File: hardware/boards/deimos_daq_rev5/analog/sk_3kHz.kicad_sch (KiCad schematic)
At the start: 6 parts, among them U45001 OPA333xxDBV

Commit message: put +/12V on all inamps. add 3.3V zener behind first resistor of each filter.
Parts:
- added D15001: BZT52C3V3, Diode_SMD:D_SOD-323, symbol Device:D_Zener
- renumbered C45001 to C29001, C45002 to C29002, C45003 to C29003, R45001 to R29001, R45002 to R29002, U45001 to U29001
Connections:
- net GND: now also D15001.2 (A)
- net at C29002.1, R29001.2, R29002.1: now also D15001.1 (K)

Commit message: add stabilizing integrator to current sinks
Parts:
- renumbered C29001 to C27001, C29002 to C27002, C29003 to C27003, D15001 to D17001, R29001 to R27001, R29002 to R27002, U29001 to U27001
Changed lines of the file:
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@@
 		(on_board yes)
 		(dnp no)
-		(property "Reference" "C29001"
+		(property "Reference" "C27001"
 			(at 98.552 96.774 90)
 			(effects
@@
 		(on_board yes)
 		(dnp no)
-		(property "Reference" "C29003"
+		(property "Reference" "C27003"
 			(at 116.078 76.2 90)
 			(effects
@@
 		(on_board yes)
 		(dnp no)
-		(property "Reference" "R29001"
+		(property "Reference" "R27001"
 			(at 82.55 77.343 90)
 			(effects
@@
 		(on_board yes)
 		(dnp no)
-		(property "Reference" "#PWR193"
+		(property "Reference" "#PWR188"
 			(at 113.03 99.06 0)
 			(effects
@@
 		(on_board yes)
 		(dnp no)
-		(property "Reference" "D15001"
+		(property "Reference" "D17001"
 			(at 85.09 86.614 0)
 			(effects
@@
 		(on_board yes)
 		(dnp no)
-		(property "Reference" "U29001"
+		(property "Reference" "U27001"
 			(at 121.158 89.916 0)
 			(effects
@@
 		(on_board yes)
 		(dnp no)
-		(property "Reference" "#PWR192"
+		(property "Reference" "#PWR187"
 			(at 120.65 83.82 0)
 			(effects
@@
 		(on_board yes)
 		(dnp no)
-		(property "Reference" "R29002"
+		(property "Reference" "R27002"
 			(at 93.98 77.343 90)
 			(effects
@@
 		(on_board yes)
 		(dnp no)
-		(property "Reference" "#PWR15005"
+		(property "Reference" "#PWR17005"
 			(at 87.376 96.52 0)
 			(effects
@@
 		(on_board yes)
 		(dnp no)
-		(property "Reference" "C29002"
+		(property "Reference" "C27002"
 			(at 110.998 58.674 0)
 			(effects
@@
 		(on_board yes)
 		(dnp no)
-		(property "Reference" "#PWR191"
+		(property "Reference" "#PWR186"
 			(at 116.84 72.39 0)
 			(effects
@@
 		(on_board yes)
 		(dnp no)
-		(property "Reference" "#PWR190"
+		(property "Reference" "#PWR185"
 			(at 101.6 99.06 0)
 			(effects

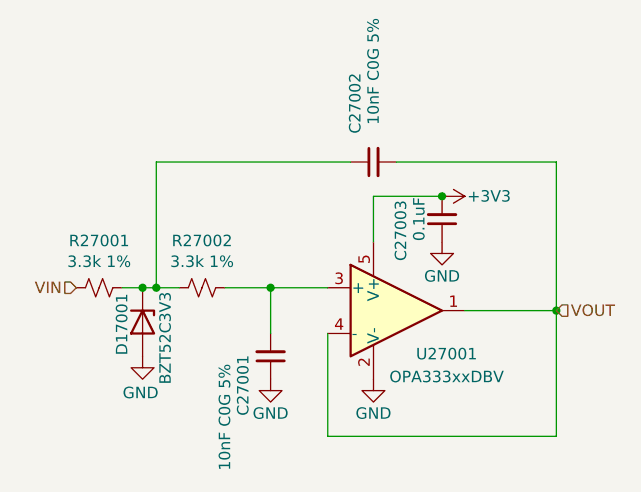
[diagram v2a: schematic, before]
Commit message: use opa196 with split rail instead of opa333 with single rail. replace zeners.
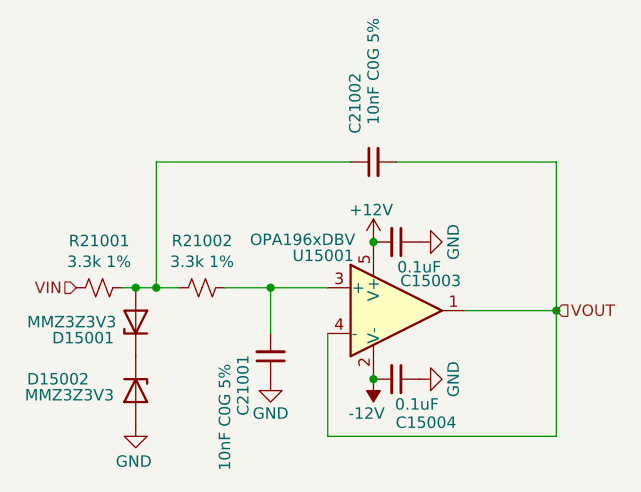
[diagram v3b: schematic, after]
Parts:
- removed C27003: 0.1uF, Capacitor_SMD:C_0402_1005Metric, symbol Device:C_Small
- removed D17001: BZT52C3V3, Diode_SMD:D_SOD-323, symbol Device:D_Zener
- removed U27001: OPA333xxDBV, Package_TO_SOT_SMD:SOT-23-5, symbol Amplifier_Operational:OPA333xxDBV
- added C15003, C15004: 0.1uF, Capacitor_SMD:C_0402_1005Metric, symbol Device:C_Small
- added D15001, D15002: MMZ3Z3V3, Diode_SMD:D_SOD-323, symbol Device:D_Zener
- added U15001: OPA196xDBV, Package_TO_SOT_SMD:SOT-23-5, symbol Amplifier_Operational:OPA196xDBV
- renumbered C27001 to C21001, C27002 to C21002, R27001 to R21001, R27002 to R21002
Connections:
- net GND: now also C15003.1, C15004.1, D15002.2 (A)
- net VOUT: now also U15001.1, U15001.4 (-)
- net at C21001.2, R21002.2: now also U15001.3 (+)
- net at C21002.1, R21001.2, R21002.1: now also D15001.2 (A)
- new net: D15001.1 (K), D15002.1 (K)
- new net +12V: C15003.2, U15001.5 (V+)
- new net -12V: C15004.2, U15001.2 (V-)

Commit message: remove unnecessary amps and buffers
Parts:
- renumbered C15003 to C17003, C15004 to C17004, C21001 to C47001, C21002 to C47002, D15001 to D17001, D15002 to D17002, R21001 to R47001, R21002 to R47002, U15001 to U17001
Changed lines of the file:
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@@
 		(on_board yes)
 		(dnp no)
-		(property "Reference" "#PWR15004"
+		(property "Reference" "#PWR17004"
 			(at 113.03 88.9 0)
 			(effects
@@
 		(on_board yes)
 		(dnp no)
-		(property "Reference" "C21001"
+		(property "Reference" "C47001"
 			(at 98.552 96.774 90)
 			(effects
@@
 		(on_board yes)
 		(dnp no)
-		(property "Reference" "D15002"
+		(property "Reference" "D17002"
 			(at 77.978 92.71 90)
 			(effects
@@
 		(on_board yes)
 		(dnp no)
-		(property "Reference" "D15001"
+		(property "Reference" "D17001"
 			(at 80.772 88.138 90)
 			(effects
@@
 		(on_board yes)
 		(dnp no)
-		(property "Reference" "#PWR15002"
+		(property "Reference" "#PWR17002"
 			(at 86.614 104.14 0)
 			(effects
@@
 		(on_board yes)
 		(dnp no)
-		(property "Reference" "R21001"
+		(property "Reference" "R47001"
 			(at 82.55 77.343 90)
 			(effects
@@
 		(on_board yes)
 		(dnp no)
-		(property "Reference" "#PWR15006"
+		(property "Reference" "#PWR17006"
 			(at 124.46 92.71 0)
 			(effects
@@
 		(on_board yes)
 		(dnp no)
-		(property "Reference" "#PWR15005"
+		(property "Reference" "#PWR17005"
 			(at 124.46 77.47 0)
 			(effects
@@
 		(on_board yes)
 		(dnp no)
-		(property "Reference" "U15001"
+		(property "Reference" "U17001"
 			(at 107.442 78.994 0)
 			(effects
@@
 		(on_board yes)
 		(dnp no)
-		(property "Reference" "R21002"
+		(property "Reference" "R47002"
 			(at 93.98 77.343 90)
 			(effects
@@
 		(on_board yes)
 		(dnp no)
-		(property "Reference" "C15003"
+		(property "Reference" "C17003"
 			(at 119.38 81.788 90)
 			(effects
@@
 		(on_board yes)
 		(dnp no)
-		(property "Reference" "C15004"
+		(property "Reference" "C17004"
 			(at 118.872 97.536 90)
 			(effects
@@
 		(on_board yes)
 		(dnp no)
-		(property "Reference" "C21002"
+		(property "Reference" "C47002"
 			(at 110.998 58.674 0)
 			(effects
@@
 		(on_board yes)
 		(dnp no)
-		(property "Reference" "#PWR15003"
+		(property "Reference" "#PWR17003"
 			(at 113.03 81.28 0)
 			(effects
@@
 		(on_board yes)
 		(dnp no)
-		(property "Reference" "#PWR169"
+		(property "Reference" "#PWR259"
 			(at 101.6 99.06 0)
 			(effects

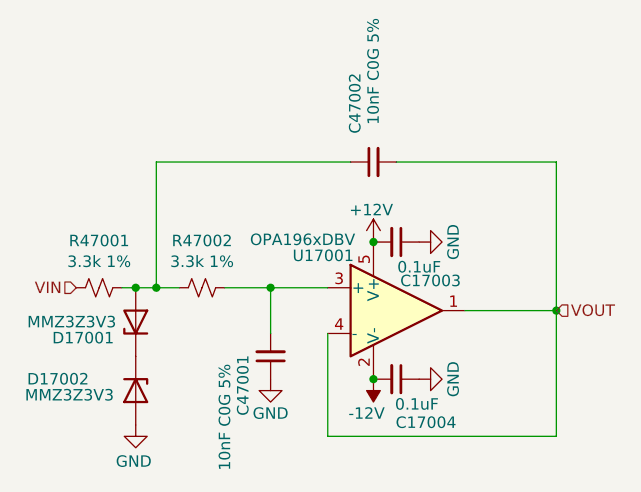
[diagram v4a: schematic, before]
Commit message: wip to update layout for controller base
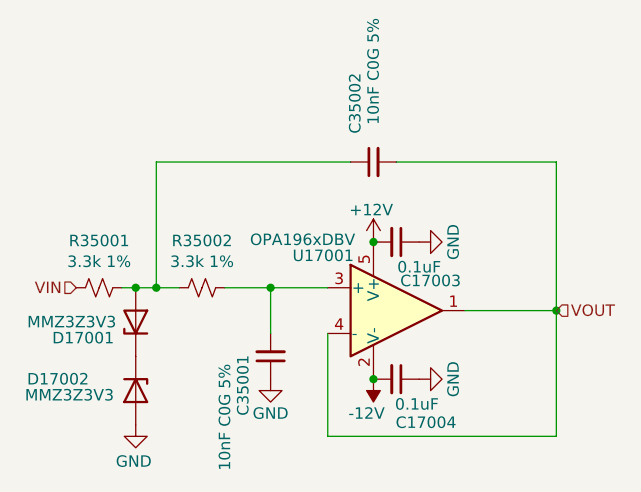
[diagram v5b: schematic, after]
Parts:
- renumbered C47001 to C35001, C47002 to C35002, R47001 to R35001, R47002 to R35002
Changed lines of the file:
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@@
 		(on_board yes)
 		(dnp no)
-		(property "Reference" "C47001"
+		(property "Reference" "C35001"
 			(at 98.552 96.774 90)
 			(effects
@@
 		(on_board yes)
 		(dnp no)
-		(property "Reference" "R47001"
+		(property "Reference" "R35001"
 			(at 82.55 77.343 90)
 			(effects
@@
 		(on_board yes)
 		(dnp no)
-		(property "Reference" "R47002"
+		(property "Reference" "R35002"
 			(at 93.98 77.343 90)
 			(effects
@@
 		(on_board yes)
 		(dnp no)
-		(property "Reference" "C47002"
+		(property "Reference" "C35002"
 			(at 110.998 58.674 0)
 			(effects
@@
 		(on_board yes)
 		(dnp no)
-		(property "Reference" "#PWR259"
+		(property "Reference" "#PWR205"
 			(at 101.6 99.06 0)
 			(effects

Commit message: eliminate 5V supply
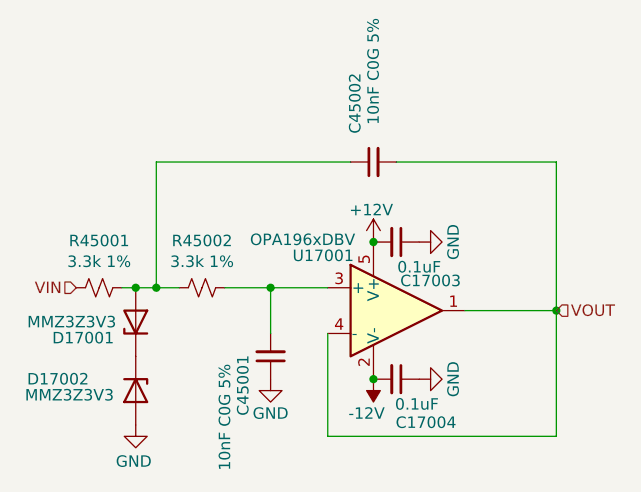
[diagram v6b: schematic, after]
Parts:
- renumbered C35001 to C45001, C35002 to C45002, R35001 to R45001, R35002 to R45002
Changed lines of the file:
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@@
 		(on_board yes)
 		(dnp no)
-		(property "Reference" "C35001"
+		(property "Reference" "C45001"
 			(at 98.552 96.774 90)
 			(effects
@@
 		(on_board yes)
 		(dnp no)
-		(property "Reference" "R35001"
+		(property "Reference" "R45001"
 			(at 82.55 77.343 90)
 			(effects
@@
 		(on_board yes)
 		(dnp no)
-		(property "Reference" "R35002"
+		(property "Reference" "R45002"
 			(at 93.98 77.343 90)
 			(effects
@@
 		(on_board yes)
 		(dnp no)
-		(property "Reference" "C35002"
+		(property "Reference" "C45002"
 			(at 110.998 58.674 0)
 			(effects
@@
 		(on_board yes)
 		(dnp no)
-		(property "Reference" "#PWR205"
+		(property "Reference" "#PWR250"
 			(at 101.6 99.06 0)
 			(effects

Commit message: wip to update layout for voltage inputs
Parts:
- renumbered C45001 to C27001, C45002 to C27002, R45001 to R27001, R45002 to R27002
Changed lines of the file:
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@@
 		(on_board yes)
 		(dnp no)
-		(property "Reference" "C45001"
+		(property "Reference" "C27001"
 			(at 98.552 96.774 90)
 			(effects
@@
 		(on_board yes)
 		(dnp no)
-		(property "Reference" "R45001"
+		(property "Reference" "R27001"
 			(at 82.55 77.343 90)
 			(effects
@@
 		(on_board yes)
 		(dnp no)
-		(property "Reference" "R45002"
+		(property "Reference" "R27002"
 			(at 93.98 77.343 90)
 			(effects
@@
 		(on_board yes)
 		(dnp no)
-		(property "Reference" "C45002"
+		(property "Reference" "C27002"
 			(at 110.998 58.674 0)
 			(effects
@@
 		(on_board yes)
 		(dnp no)
-		(property "Reference" "#PWR250"
+		(property "Reference" "#PWR185"
 			(at 101.6 99.06 0)
 			(effects

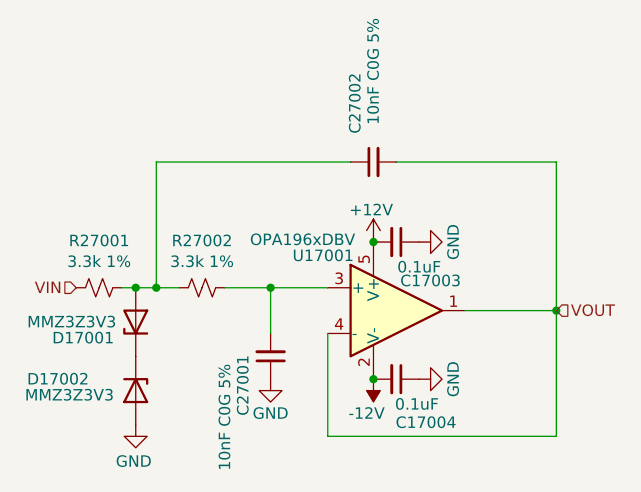
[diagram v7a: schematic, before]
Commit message: finish first pass of component layout for frontend
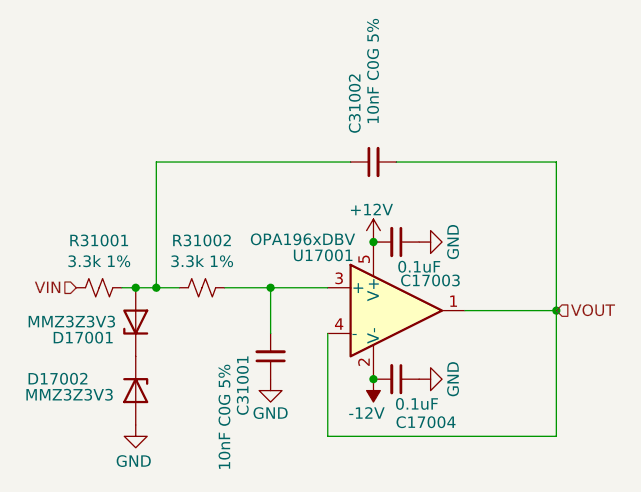
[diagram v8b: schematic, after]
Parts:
- renumbered C27001 to C31001, C27002 to C31002, R27001 to R31001, R27002 to R31002
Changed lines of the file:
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@@
 		(on_board yes)
 		(dnp no)
-		(property "Reference" "C27001"
+		(property "Reference" "C31001"
 			(at 98.552 96.774 90)
 			(effects
@@
 		(on_board yes)
 		(dnp no)
-		(property "Reference" "R27001"
+		(property "Reference" "R31001"
 			(at 82.55 77.343 90)
 			(effects
@@
 		(on_board yes)
 		(dnp no)
-		(property "Reference" "R27002"
+		(property "Reference" "R31002"
 			(at 93.98 77.343 90)
 			(effects
@@
 		(on_board yes)
 		(dnp no)
-		(property "Reference" "C27002"
+		(property "Reference" "C31002"
 			(at 110.998 58.674 0)
 			(effects
@@
 		(on_board yes)
 		(dnp no)
-		(property "Reference" "#PWR185"
+		(property "Reference" "#PWR195"
 			(at 101.6 99.06 0)
 			(effects
